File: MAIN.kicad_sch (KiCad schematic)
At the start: 45 parts, among them J1 USB_C_Receptacle_USB2.0_16P, J2 Conn_01x02_Socket, SW1 SW_Push, SW2 SW_Push, SW3 SW_Push, SW4 SW_Push, SW5 SW_Push, U1 USBLC6-2SC6, U2 ESP32-S3-MINI-1, U3 MP2667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

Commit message: Layout completed
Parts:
- added J3: Conn_01x03, Connector_PinHeader_2.54mm:PinHeader_1x03_P2.54mm_Vertical, symbol Connector_Generic:Conn_01x03
- SW2, SW4: footprint Button_Switch_SMD:SW_SPST_TS-1088-xR020 -> Button_Switch_SMD:SW_SPST_TL3305C
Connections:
- net BATT_CLK: now also U2.9 (IO5); no longer U2.31 (IO35)
- net BATT_DATA: now also U2.8 (IO4); no longer U2.29 (IO34)
- net GND: now also SW2.1, J3.3 (Pin_3); no longer SW2.2
- net GPS/MAG_CLK: now also U2.18 (IO14); no longer U2.10 (IO6)
- net GPS/MAG_DATA: now also U2.17 (IO13); no longer U2.9 (IO5)
- net MAG_INT: now also U2.16 (IO12); no longer U2.20 (IO16)
- net OLED_CS: now also U2.26 (IO26); no longer U2.11 (IO7)
- net OLED_DC: now also U2.28 (IO33); no longer U2.8 (IO4)
- net OLED_RST: now also U2.29 (IO34); no longer U2.26 (IO26)
- net OLED/SD_MOSI: now also U2.22 (IO18); no longer U2.15 (IO11)
- net OLED/SD_SCK: now also U2.21 (IO17); no longer U2.16 (IO12)
- net SD_CS: now also U2.25 (IO21); no longer U2.14 (IO10)
- net SD_DETECT: now also U2.19 (IO15); no longer U2.13 (IO9)
- net SD_MISO: now also U2.20 (IO16); no longer U2.17 (IO13)
- net +BATT: now reaches C9.2, J2.2 (Pin_2), TP6.1, U3.8 (BATT), U3.9 (BATT)
- net SW_TOGGLE: now reaches C2.1, R3.1
- net SW_TOGGLE: now also SW2.2, U2.35 (IO39); no longer SW2.1, U2.22 (IO18)
- net SW_PWR: now reaches C6.1, R11.1, SW4.1
- net SW_PWR: now also U2.34 (IO38); no longer U2.38 (IO42)
- net SW_LOG: now reaches C7.1, R12.1, SW5.1
- net SW_LOG: now also U2.33 (IO37); no longer U2.25 (IO21)
- net at U2.12 (IO8): no longer R2.1
- net TX: now reaches U2.39 (TXD0)
- net TX: now also TP2.1, J3.1 (Pin_1)
- net RX: now reaches U2.40 (RXD0)
- net RX: now also TP3.1, J3.2 (Pin_2)
- net at U2.6 (IO2): now also R2.1
- net INT renamed BATT_INT
- net BATT_INT: now also U2.10 (IO6)
- net USB_N: no longer names the net of U1.6 (I/O1)
- net USB_N: no longer U2.23 (USB_D-)
- net USB_P: no longer names the net of U1.4 (I/O2)
- net USB_P: no longer U2.24 (USB_D+)
- now unconnected: J1.A6 (D+), J1.A7 (D-), J1.B6 (D+), J1.B7 (D-), U1.1 (I/O1), U1.3 (I/O2)
- no-connect marks 21 -> 28
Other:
- note added: "(board) TX -> RX (external) (board) RX -> TX (external)"
- note added: "External Programmer to reduce BOM and board size FTDI adapter"
- moved on the sheet: C2, C6, C7, R11, R12, R3, R5, R6, SW5

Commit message: modified layout
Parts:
- added TP9: TestPoint, TestPoint:TestPoint_Pad_D1.5mm, symbol Connector:TestPoint
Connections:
- net GND: now also TP9.1
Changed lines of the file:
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@@
 	(text "(board) TX -> RX (external)\n(board) RX -> TX (external)"
 		(exclude_from_sim no)
-		(at 145.542 107.442 0)
+		(at 147.828 105.41 0)
 		(effects
 			(font
@@
 	(text "External Programmer to reduce BOM and board size\nFTDI adapter \n"
 		(exclude_from_sim no)
-		(at 144.526 102.362 0)
+		(at 146.812 100.33 0)
 		(effects
 			(font
@@
 	)
 	(symbol
+		(lib_id "Connector:TestPoint")
+		(at 107.95 176.53 270)
+		(unit 1)
+		(exclude_from_sim no)
+		(in_bom yes)
+		(on_board yes)
+		(dnp no)
+		(property "Reference" "TP9"
+			(at 113.284 177.8 0)
+			(effects
+				(font
+					(size 1.27 1.27)
+				)
+				(justify right)
+			)
+		)
+		(property "Value" "TestPoint"
+			(at 114.3 177.546 0)
+			(effects
+				(font
+					(size 1.27 1.27)
+				)
+				(justify right)
+				(hide yes)
+			)
+		)
+		(property "Footprint" "TestPoint:TestPoint_Pad_D1.5mm"
+			(at 107.95 181.61 0)
+			(effects
+				(font
+					(size 1.27 1.27)
+				)
+				(hide yes)
+			)
+		)
+		(property "Datasheet" "~"
+			(at 107.95 181.61 0)
+			(effects
+				(font
+					(size 1.27 1.27)
+				)
+				(hide yes)
+			)
+		)
+		(property "Description" "test point"
+			(at 107.95 176.53 0)
+			(effects
+				(font
+					(size 1.27 1.27)
+				)
+				(hide yes)
+			)
+		)
+		(property "LCSC" ""
+			(at 107.95 176.53 0)
+			(effects
+				(font
+					(size 1.27 1.27)
+				)
+				(hide yes)
+			)
+		)
+		(property "MPN" ""
+			(at 107.95 176.53 0)
+			(effects
+				(font
+					(size 1.27 1.27)
+				)
+				(hide yes)
+			)
+		)
+		(property "Manufacturer" ""
+			(at 107.95 176.53 0)
+			(effects
+				(font
+					(size 1.27 1.27)
+				)
+				(hide yes)
+			)
+		)
+		(pin "1"
+		)
+		(instances
+			(project "ESP32_Tracker"
+				(path "/92195c42-0bc4-473e-a890-6f85786d3c69/b4df9ef1-8ff4-45c1-a208-fa7b3317f92b"
+					(reference "TP9")
+					(unit 1)
+				)
+			)
+		)
+	)
+	(symbol
 		(lib_id "power:+3.3V")
 		(at 180.34 41.91 0)
@@
 		)
 		(property "Value" "+3.3V"
-			(at 125.73 46.736 0)
+			(at 125.73 47.244 0)
 			(effects
 				(font

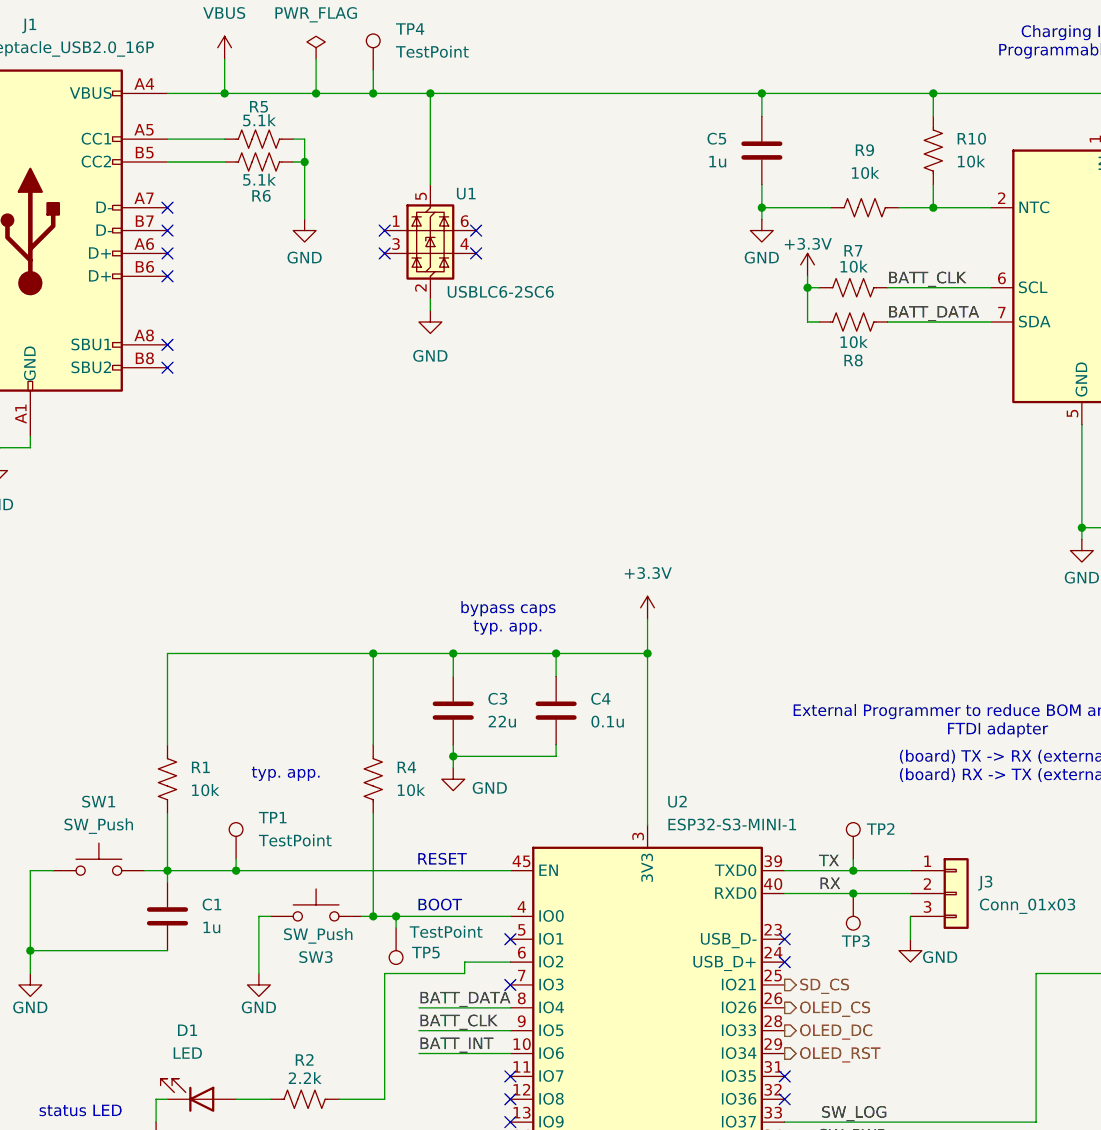
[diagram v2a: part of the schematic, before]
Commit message: added USBC programming
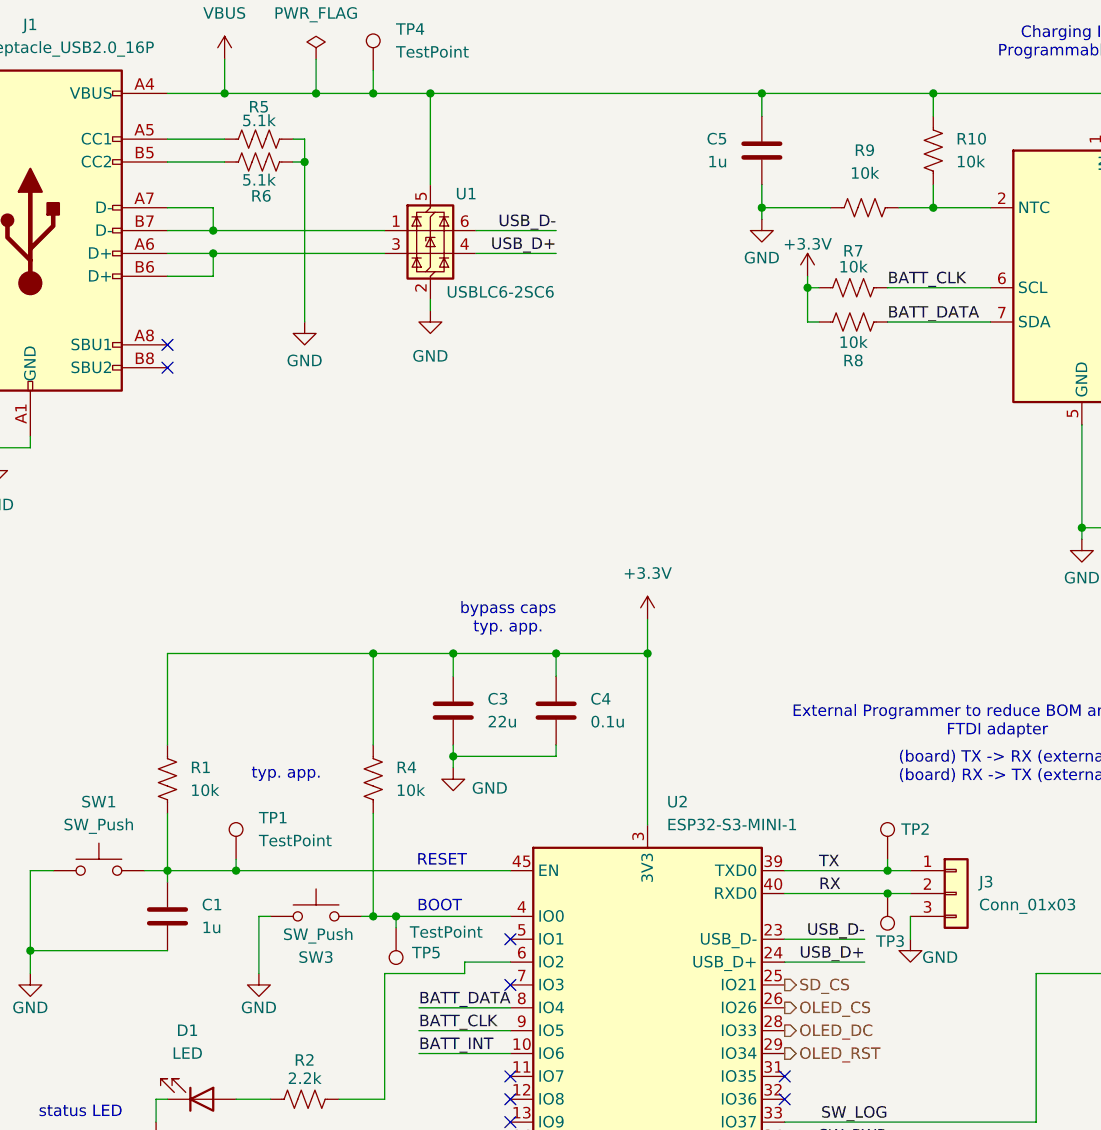
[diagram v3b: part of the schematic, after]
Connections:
- net at J1.A6 (D+): now also J1.B6 (D+), U1.3 (I/O2)
- net at J1.A7 (D-): now also J1.B7 (D-), U1.1 (I/O1)
- net USB_D+: now reaches U1.4 (I/O2)
- net USB_D+: now also U2.24 (USB_D+)
- net USB_D-: now reaches U1.6 (I/O1)
- net USB_D-: now also U2.23 (USB_D-)
- no-connect marks 28 -> 18
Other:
- moved on the sheet: TP2, TP3

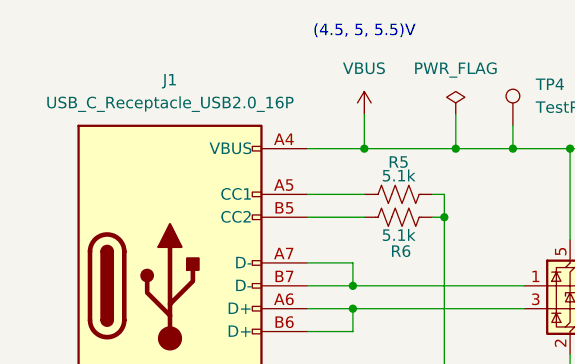
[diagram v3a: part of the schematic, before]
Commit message: modified BOM
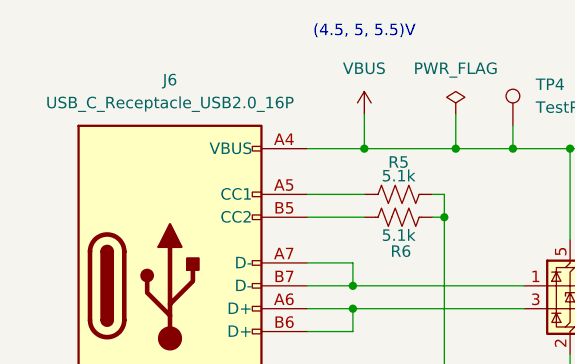
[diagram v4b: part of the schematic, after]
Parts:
- removed J1: USB_C_Receptacle_USB2.0_16P, Connector_USB:USB_C_Receptacle_G-Switch_GT-USB-7010ASV, symbol Connector:USB_C_Receptacle_USB2.0_16P
- added J6: USB_C_Receptacle_USB2.0_16P, Connector_USB:USB_C_Receptacle_GCT_USB4105-xx-A_16P_TopMnt_Horizontal, symbol Connector:USB_C_Receptacle_USB2.0_16P
- SW2, SW4, SW5: Distributor Link https://www.lcsc.com/product-detail/C720477.html?s_z=n_push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 -> https://www.digikey.com/en/products/detail/e-switch/TL3305C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; LCSC C720477 -> (none); MPN TS-1088-AR02016 -> TL3305CF260QG; Manufacturer XUNPU -> E-Switch
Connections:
- net GND: now also J6.A1 (GND), J6.A12 (GND), J6.B1 (GND), J6.B12 (GND), J6.S1 (SHIELD)
- net VBUS: now also J6.A4 (VBUS), J6.A9 (VBUS), J6.B4 (VBUS), J6.B9 (VBUS)
- net at R5.2: now also J6.A5 (CC1)
- net at U1.3 (I/O2): now also J6.A6 (D+), J6.B6 (D+)
- net at U1.1 (I/O1): now also J6.A7 (D-), J6.B7 (D-)
- net at R6.1: now also J6.B5 (CC2)
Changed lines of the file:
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@@
 	)
 	(symbol
-		(lib_id "Connector:USB_C_Receptacle_USB2.0_16P")
-		(at 39.37 45.72 0)
-		(unit 1)
-		(exclude_from_sim no)
-		(in_bom yes)
-		(on_board yes)
-		(dnp no)
-		(fields_autoplaced yes)
-		(property "Reference" "J1"
-			(at 39.37 22.86 0)
-			(effects
-				(font
-					(size 1.27 1.27)
-				)
-			)
-		)
-		(property "Value" "USB_C_Receptacle_USB2.0_16P"
-			(at 39.37 25.4 0)
-			(effects
-				(font
-					(size 1.27 1.27)
-				)
-			)
-		)
-		(property "Footprint" "Connector_USB:USB_C_Receptacle_G-Switch_GT-USB-7010ASV"
-			(at 43.18 45.72 0)
-			(effects
-				(font
-					(size 1.27 1.27)
-				)
-				(hide yes)
-			)
-		)
-		(property "Datasheet" "https://www.lcsc.com/datasheet/C2988369.pdf"
-			(at 43.18 45.72 0)
-			(effects
-				(font
-					(size 1.27 1.27)
-				)
-				(hide yes)
-			)
-		)
-		(property "Description" "USB 2.0-only 16P Type-C Receptacle connector"
-			(at 39.37 45.72 0)
-			(effects
-				(font
-					(size 1.27 1.27)
-				)
-				(hide yes)
-			)
-		)
-		(property "LCSC" "C2988369"
-			(at 39.37 45.72 0)
-			(effects
-				(font
-					(size 1.27 1.27)
-				)
-				(hide yes)
-			)
-		)
-		(property "MPN" "GT-USB-7010ASV"
-			(at 39.37 45.72 0)
-			(effects
-				(font
-					(size 1.27 1.27)
-				)
-				(hide yes)
-			)
-		)
-		(property "Manufacturer" "G-Switch"
-			(at 39.37 45.72 0)
-			(effects
-				(font
-					(size 1.27 1.27)
-				)
-				(hide yes)
-			)
-		)
-		(property "Distributor Link" "https://www.lcsc.com/product-detail/C2988369.html?s_z=n_GT-USB-7010ASV"
-			(at 39.37 45.72 0)
-			(effects
-				(font
-					(size 1.27 1.27)
-				)
-				(hide yes)
-			)
-		)
-		(pin "B4"
-		)
-		(pin "A12"
-		)
-		(pin "B8"
-		)
-		(pin "B7"
-		)
-		(pin "A5"
-		)
-		(pin "B1"
-		)
-		(pin "S1"
-		)
-		(pin "B12"
-		)
-		(pin "B9"
-		)
-		(pin "B5"
-		)
-		(pin "A6"
-		)
-		(pin "A4"
-		)
-		(pin "B6"
-		)
-		(pin "A1"
-		)
-		(pin "A9"
-		)
-		(pin "A7"
-		)
-		(pin "A8"
-		)
-		(instances
-			(project "ESP32_Tracker"
-				(path "/92195c42-0bc4-473e-a890-6f85786d3c69/b4df9ef1-8ff4-45c1-a208-fa7b3317f92b"
-					(reference "J1")
-					(unit 1)
-				)
-			)
-		)
-	)
-	(symbol
 		(lib_id "Device:R_US")
 		(at 139.7 36.83 180)
@@
 	)
 	(symbol
+		(lib_id "Connector:USB_C_Receptacle_USB2.0_16P")
+		(at 39.37 45.72 0)
+		(unit 1)
+		(exclude_from_sim no)
+		(in_bom yes)
+		(on_board yes)
+		(dnp no)
+		(fields_autoplaced yes)
+		(property "Reference" "J6"
+			(at 39.37 22.86 0)
+			(effects
+				(font
+					(size 1.27 1.27)
+				)
+			)
+		)
+		(property "Value" "USB_C_Receptacle_USB2.0_16P"
+			(at 39.37 25.4 0)
+			(effects
+				(font
+					(size 1.27 1.27)
+				)
+			)
+		)
+		(property "Footprint" "Connector_USB:USB_C_Receptacle_GCT_USB4105-xx-A_16P_TopMnt_Horizontal"
+			(at 43.18 45.72 0)
+			(effects
+				(font
+					(size 1.27 1.27)
+				)
+				(hide yes)
+			)
+		)
+		(property "Datasheet" "https://www.lcsc.com/datasheet/C2988369.pdf"
+			(at 43.18 45.72 0)
+			(effects
+				(font
+					(size 1.27 1.27)
+				)
+				(hide yes)
+			)
+		)
+		(property "Description" "USB 2.0-only 16P Type-C Receptacle connector"
+			(at 39.37 45.72 0)
+			(effects
+				(font
+					(size 1.27 1.27)
+				)
+				(hide yes)
+			)
+		)
+		(property "LCSC" ""
+			(at 39.37 45.72 0)
+			(effects
+				(font
+					(size 1.27 1.27)
+				)
+				(hide yes)
+			)
+		)
+		(property "MPN" "USB4105-GF-A"
+			(at 39.37 45.72 0)
+			(effects
+				(font
+					(size 1.27 1.27)
+				)
+				(hide yes)
+			)
+		)
+		(property "Manufacturer" "GCT"
+			(at 39.37 45.72 0)
+			(effects
+				(font
+					(size 1.27 1.27)
+				)
+				(hide yes)
+			)
+		)
+		(property "Distributor Link" "https://www.digikey.com/en/products/detail/gct/USB4105-GF-A/11198441"
+			(at 39.37 45.72 0)
+			(effects
+				(font
+					(size 1.27 1.27)
+				)
+				(hide yes)
+			)
+		)
+		(pin "B4"
+		)
+		(pin "A12"
+		)
+		(pin "B8"
+		)
+		(pin "B7"
+		)
+		(pin "A5"
+		)
+		(pin "B1"
+		)
+		(pin "S1"
+		)
+		(pin "B12"
+		)
+		(pin "B9"
+		)
+		(pin "B5"
+		)
+		(pin "A6"
+		)
+		(pin "A4"
+		)
+		(pin "B6"
+		)
+		(pin "A1"
+		)
+		(pin "A9"
+		)
+		(pin "A7"
+		)
+		(pin "A8"
+		)
+		(instances
+			(project "ESP32_Tracker"
+				(path "/92195c42-0bc4-473e-a890-6f85786d3c69/b4df9ef1-8ff4-45c1-a208-fa7b3317f92b"
+					(reference "J6")
+					(unit 1)
+				)
+			)
+		)
+	)
+	(symbol
 		(lib_id "Switch:SW_Push")
 		(at 46.99 116.84 0)
@@
 			)
 		)
-		(property "LCSC" "C720477"
+		(property "LCSC" ""
 			(at 177.8 128.27 0)
 			(effects
@@
 			)
 		)
-		(property "MPN" "TS-1088-AR02016"
+		(property "MPN" "TL3305CF260QG"
 			(at 177.8 128.27 0)
 			(effects
@@
 			)
 		)
-		(property "Manufacturer" "XUNPU"
+		(property "Manufacturer" "E-Switch"
 			(at 177.8 128.27 0)
 			(effects
@@
 			)
 		)
-		(property "Distributor Link" "https://www.lcsc.com/product-detail/C720477.html?s_z=n_push%2520button%2520switch"
+		(property "Distributor Link" "https://www.digikey.com/en/products/detail/e-switch/TL3305CF260QG/5816186"
 			(at 177.8 128.27 0)
 			(effects
@@
 			)
 		)
-		(property "LCSC" "C720477"
+		(property "LCSC" ""
 			(at 214.63 147.32 0)
 			(effects
@@
 			)
 		)
-		(property "MPN" "TS-1088-AR02016"
+		(property "MPN" "TL3305CF260QG"
 			(at 214.63 147.32 0)
 			(effects
@@
 			)
 		)
-		(property "Manufacturer" "XUNPU"
+		(property "Manufacturer" "E-Switch"
 			(at 214.63 147.32 0)
 			(effects
@@
 			)
 		)
-		(property "Distributor Link" "https://www.lcsc.com/product-detail/C720477.html?s_z=n_push%2520button%2520switch"
+		(property "Distributor Link" "https://www.digikey.com/en/products/detail/e-switch/TL3305CF260QG/5816186"
 			(at 214.63 147.32 0)
 			(effects
@@
 			)
 		)
-		(property "LCSC" "C720477"
+		(property "LCSC" ""
 			(at 158.75 166.37 0)
 			(effects
@@
 			)
 		)
-		(property "MPN" "TS-1088-AR02016"
+		(property "MPN" "TL3305CF260QG"
 			(at 158.75 166.37 0)
 			(effects
@@
 			)
 		)
-		(property "Manufacturer" "XUNPU"
+		(property "Manufacturer" "E-Switch"
 			(at 158.75 166.37 0)
 			(effects
@@
 			)
 		)
-		(property "Distributor Link" "https://www.lcsc.com/product-detail/C720477.html?s_z=n_push%2520button%2520switch"
+		(property "Distributor Link" "https://www.digikey.com/en/products/detail/e-switch/TL3305CF260QG/5816186"
 			(at 158.75 166.37 0)
 			(effects
